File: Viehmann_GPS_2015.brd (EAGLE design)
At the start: 53.7 x 33 mm, 16 parts

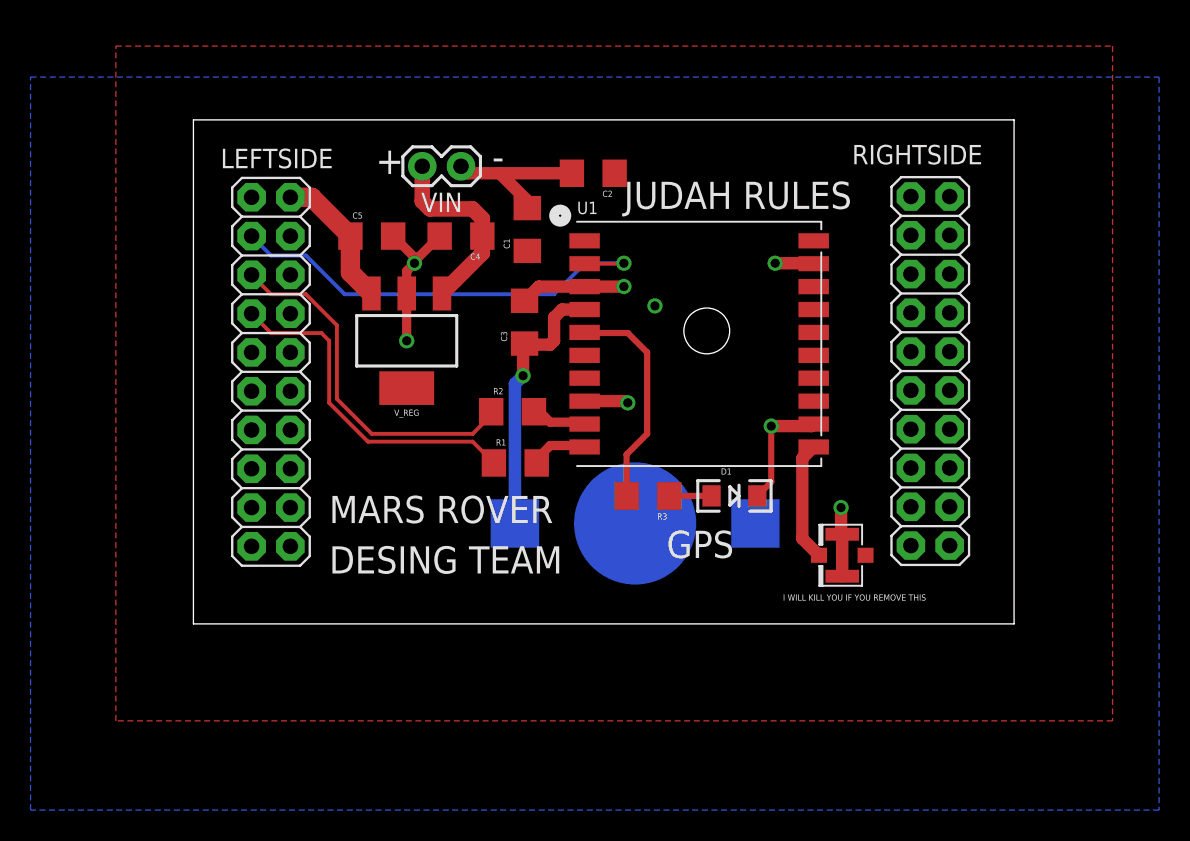
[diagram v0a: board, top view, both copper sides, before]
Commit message: Removed unnessasary files and file structure
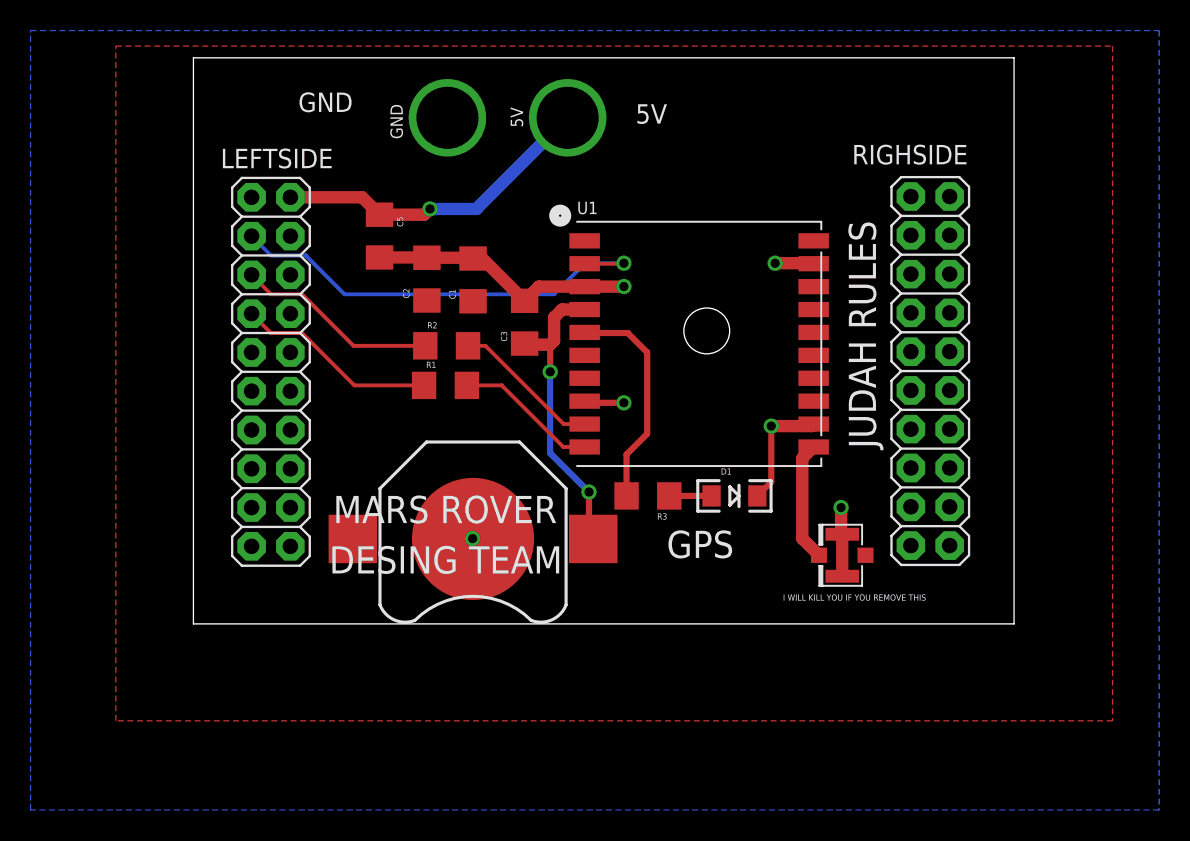
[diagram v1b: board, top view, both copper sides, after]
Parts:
- removed BATTERY: CR1220-3.7, SparkFun-Electromechanical:BATTCON_12MM
- removed C4: 1uF, SparkFun-Capacitors:1206
- removed VIN: (no value), SparkFun-Connectors:1X02
- removed V_REG: LD1117#50, SparkFun-PowerIC:SOT223
- added CR1220: 3.7V, SparkFun-Electromechanical:BATTCON_12MM
- added U$1: APP_2POS_CONFIG5V_VERT, MRDT-Connectors:APP45_5V_VERT_CONFIG
- LEFTSIDE, RIGHSIDE: value M10X2 -> (none)
- moved C2 12.9 mm to (15.3, 22.6), turned to 90 degrees
- moved R1 6.83 mm to (16.5, 15.6)
- moved R2 6.11 mm to (16.6, 18.2)
- moved C1 4.85 mm to (18.3, 22.5)
- moved C5 0.51 mm to (12.2, 25.4), turned to 270 degrees
- renumbered ANT_CONN to J1, RIGHTSIDE to RIGHSIDE
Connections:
- removed net VIN: C4.1, VIN.1, V_REG.1
- net 5V: now also U$1.5V; no longer V_REG.3
- net GND: now also CR1220.GND, U$1.GND; no longer BATTERY.GND, C4.2, VIN.2, V_REG.2
- net VBACKUP: now also CR1220.PWR@1; no longer BATTERY.PWR@1
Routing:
- net VIN: track 12.7 -> 0.00 mm
- net 5V: track 9.31 -> 21.3 mm, vias 0 -> 1
- net DATA_OUT: track 23.6 -> 13.3 mm
- net GND: track 45.0 -> 35.0 mm, vias 7 -> 6
- net DATA_IN: track 22.3 -> 13.2 mm
- net N$3: track 3.65 -> 9.76 mm
- net N$4: track 3.80 -> 9.38 mm
- net VBACKUP: track 17.9 -> 19.7 mm, vias 1 -> 2
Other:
- board size 53.7 x 33 mm -> 53.7 x 37.1 mm
- board text added: "5V"
- board text added: "GND"
- board text removed: "+"
- board text removed: "-"
